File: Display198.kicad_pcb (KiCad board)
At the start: 2 copper layers, 120.4 x 75.8 mm, 171 parts, among them J1 Y1, J10 X2, J11 X3, J12 X4, J13 X5, J14 X6, J15 X7, J16 X8, J17 X9, J18 X10, J2 Y2, J21 PL1, J22 PL2, J23 PL3, J24 PL4, J25 PL5, J26 PL6, J27 PL7, J28 PL8, J29 PL1, J3 Y3, J30 PL2, J31 PL3, J32 PL4, J33 PL5, J34 PL6, J35 PL7, J36 PL8, J4 Y4, J5 Y5, J6 Y6, J7 Y7, J8 Y8, J9 X1, U1 FQP30N06L, U10 FQP30N06L, U11 FQP30N06L, U12 FQP30N06L, U13 FQP30N06L, U14 FQP30N06L, U15 FQP30N06L, U16 FQP30N06L, U17 FQP30N06L, U18 FQP30N06L, U19 FQP30N06L, U2 FQP30N06L, U20 FQP30N06L, U21 FQP30N06L, U22 FQP30N06L, U23 FQP30N06L, U24 FQP30N06L, U25 FQP30N06L, U26 FQP30N06L, U27 FQP30N06L, U28 FQP30N06L, U29 FQP30N06L, U3 FQP30N06L, U30 FQP30N06L, U31 FQP30N06L, U32 FQP30N06L, U33 FQP30N06L, U34 FQP30N06L, U4 FQP30N06L, U5 FQP30N06L, U6 FQP30N06L, U7 FQP30N06L, U8 FQP30N06L, U9 FQP30N06L

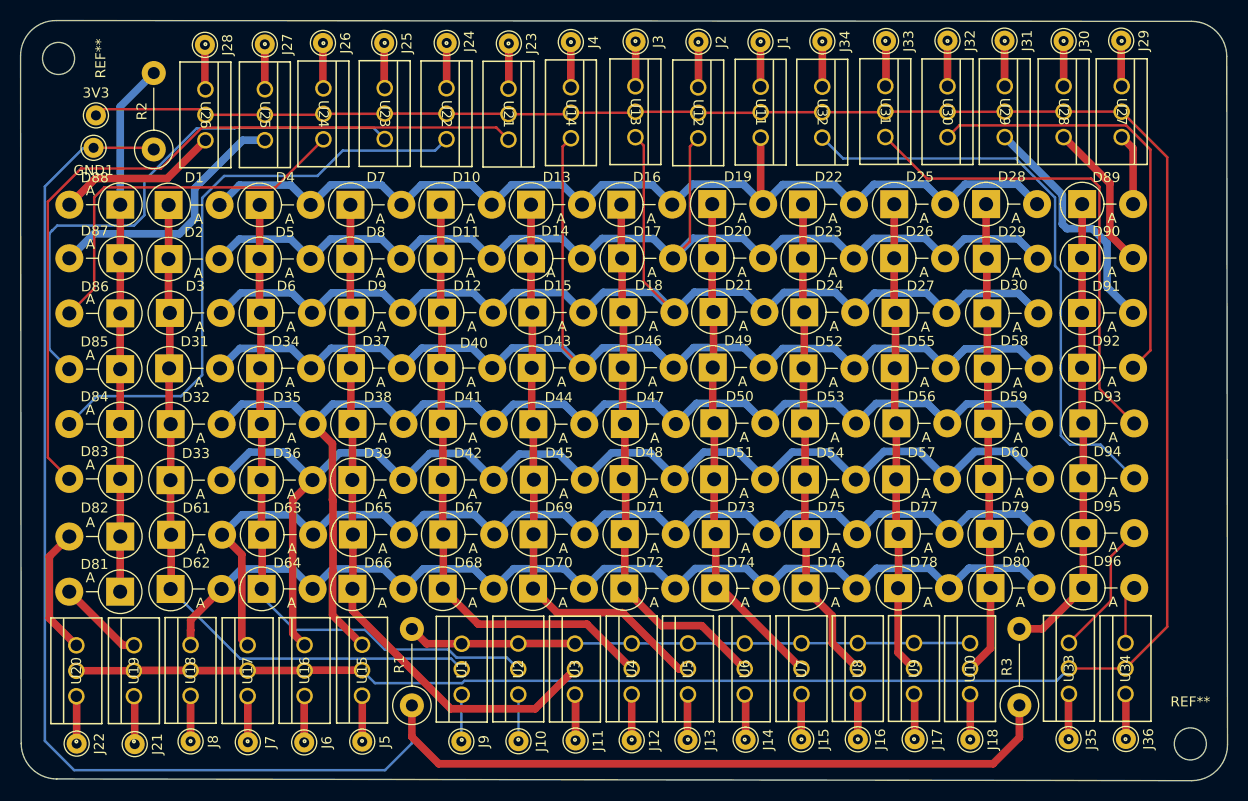
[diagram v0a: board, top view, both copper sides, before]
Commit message: changed all track widths to 20mils
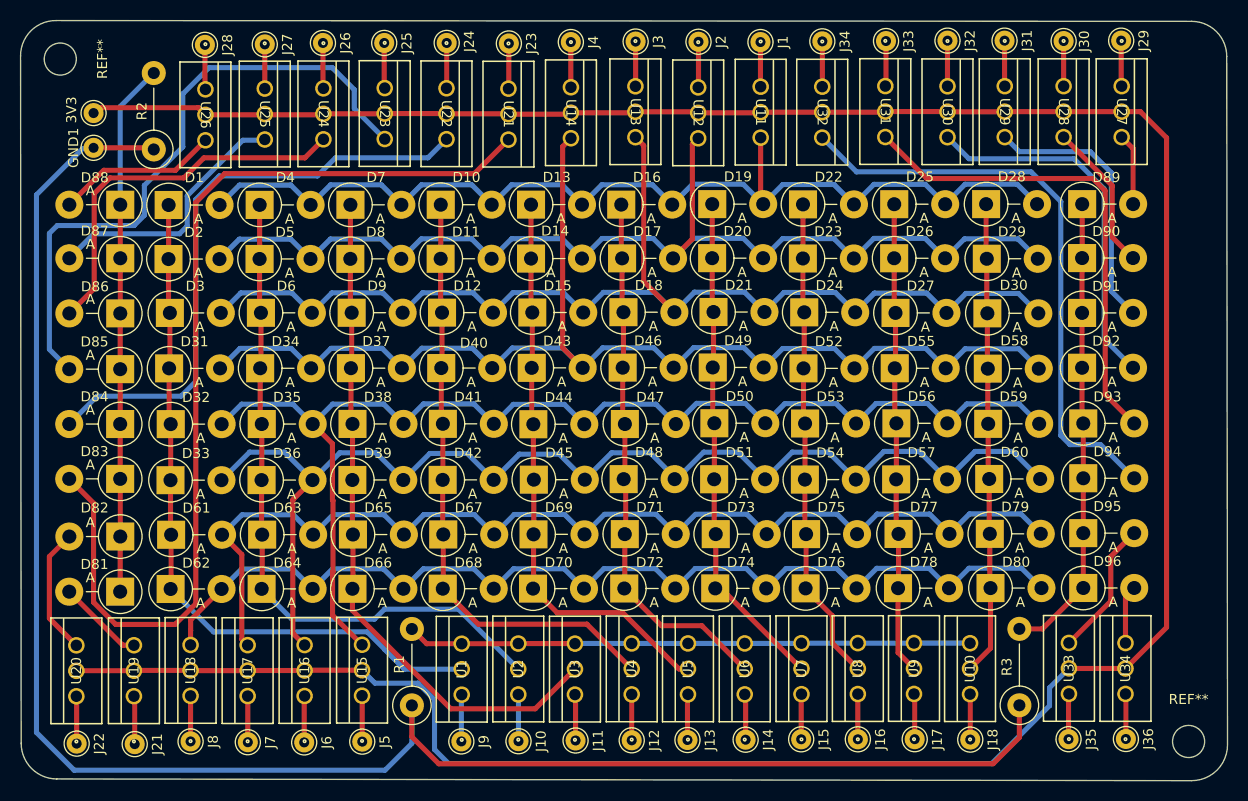
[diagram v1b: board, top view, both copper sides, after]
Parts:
- moved 3V3 0.33 mm to (99.0, 65.5)
- moved REF** 0.30 mm to (208.2, 128.2)
- moved REF** 0.18 mm to (95.7, 60.1)
- moved U25 0.07 mm to (116.1, 63.1)
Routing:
- net Net-(D83-A): track 78.0 -> 99.1 mm
- net +3V3: track 268.6 -> 280.3 mm
- net Net-(D85-A): track 54.6 -> 63.5 mm
- net Net-(D92-A): track 44.2 -> 36.8 mm
- net Net-(D91-A): track 24.3 -> 27.0 mm
- net GND: track 179.6 -> 180.3 mm
